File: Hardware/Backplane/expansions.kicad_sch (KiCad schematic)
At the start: 8 parts, among them U102 TCA9548APWR, U2901 P2X8C4M64P, U3001 NL17SZS11DFT2G-Q, U3002 NL17SZS11DFT2G-Q

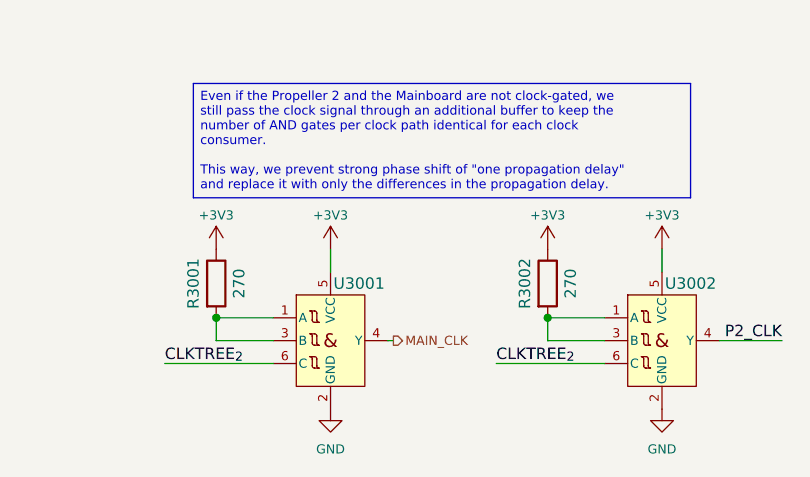
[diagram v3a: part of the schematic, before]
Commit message: Cleans up schematic even more, consolidates 270 and 100 Ohm resistors into the 560 ohm resistor, as they were only used as series resistors for the mosfets and LED current limiters
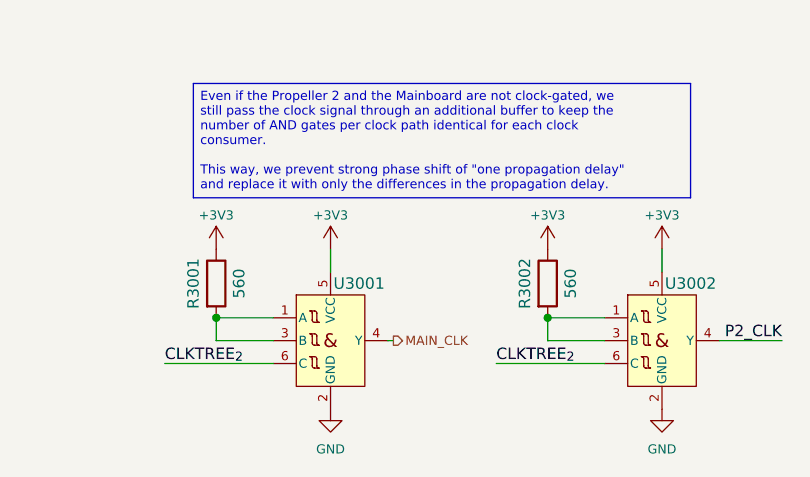
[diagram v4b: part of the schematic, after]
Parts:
- R3001, R3002: value 270 -> 560; Digikey Part No RMCF0603FT270RCT-ND -> RR08P560DCT-ND
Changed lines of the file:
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@@
 			)
 		)
-		(property "Value" "270"
+		(property "Value" "560"
 			(at 85.09 174.625 90)
 			(effects
@@
 			)
 		)
-		(property "Datasheet" "https://www.seielect.com/catalog/SEI-RMCF_RMCP.pdf"
+		(property "Datasheet" "https://www.susumu.co.jp/common/pdf/n_catalog_partition05_en.pdf"
 			(at 82.55 174.625 0)
 			(effects
@@
 			)
 		)
-		(property "Digikey Part No" "RMCF0603FT270RCT-ND"
+		(property "Digikey Part No" "RR08P560DCT-ND"
 			(at 82.55 174.625 90)
 			(effects
@@
 			)
 		)
-		(property "Value" "270"
+		(property "Value" "560"
 			(at 121.92 174.625 90)
 			(effects
@@
 			)
 		)
-		(property "Datasheet" "https://www.seielect.com/catalog/SEI-RMCF_RMCP.pdf"
+		(property "Datasheet" "https://www.susumu.co.jp/common/pdf/n_catalog_partition05_en.pdf"
 			(at 119.38 174.625 0)
 			(effects
@@
 			)
 		)
-		(property "Digikey Part No" "RMCF0603FT270RCT-ND"
+		(property "Digikey Part No" "RR08P560DCT-ND"
 			(at 119.38 174.625 90)
 			(effects

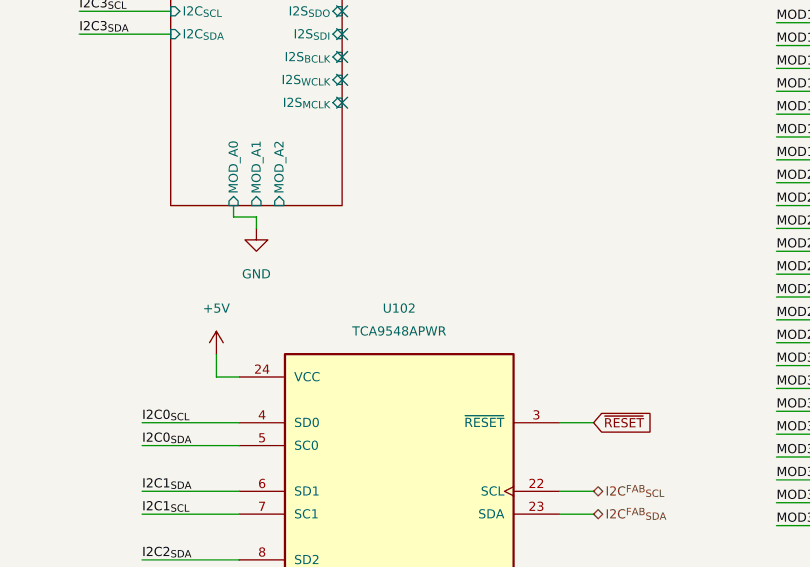
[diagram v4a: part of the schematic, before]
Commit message: More BOM consolidation
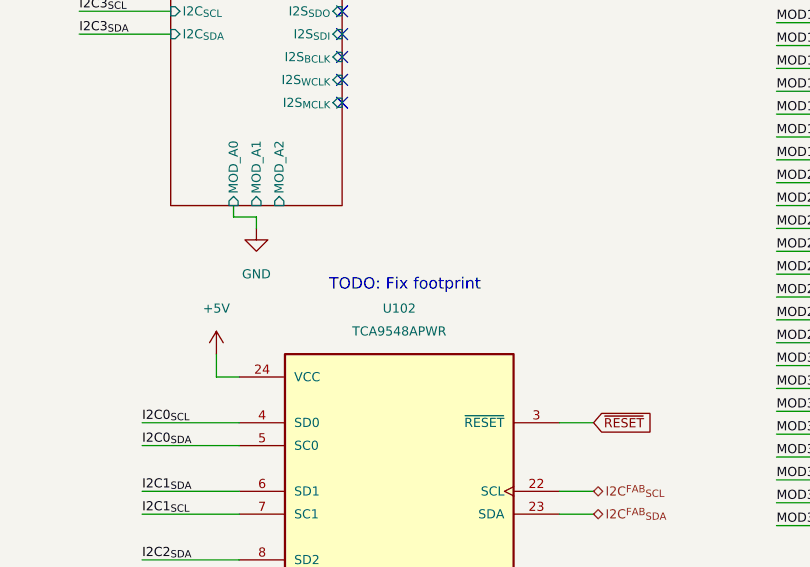
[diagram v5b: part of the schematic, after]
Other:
- note added: "TODO: Fix footprint"
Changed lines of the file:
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@@
 		(company "Ashet Technologies")
+	)
+	(text "TODO: Fix footprint"
+		(exclude_from_sim no)
+		(at 184.785 81.28 0)
+		(effects
+			(font
+				(size 1.27 1.27)
+			)
+		)
 	)
 	(text_box "Even if the Propeller 2 and the Mainboard are not clock-gated, we still pass the clock signal through an additional buffer to keep the number of AND gates per clock path identical for each clock consumer.\n\nThis way, we prevent strong phase shift of \"one propagation delay\" and replace it with only the differences in the propagation delay."

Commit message: Upgrades schematic files to KiCAD 10.0
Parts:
- U3001, U3002: DigiKey Part No 488-NL17SZS11DFT2G-QCT-ND -> (none); Digikey Part No (none) -> 488-NL17SZS11DFT2G-QCT-ND

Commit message: Further backplane PCB cleanup.
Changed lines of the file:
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@@
+	(wire
+		(pts
+			(xy 0.0762 0.0762) (xy 47.0662 0.0762)
+		)
+		(stroke
+			(width 0)
+			(type default)
+		)
+	)
 	(wire
 		(pts
@@
 		)
 		(stroke
+			(width 0)
+			(type default)
+		)
+	)
+	(wire
+		(pts
+			(xy 1.3462 1.3462) (xy 48.3362 1.3462)
+		)
+		(stroke
+			(width 0)
+			(type default)
+		)
+	)
+	(wire
+		(pts
+			(xy 0.0762 2.6162) (xy 47.0662 2.6162)
+		)
+		(stroke

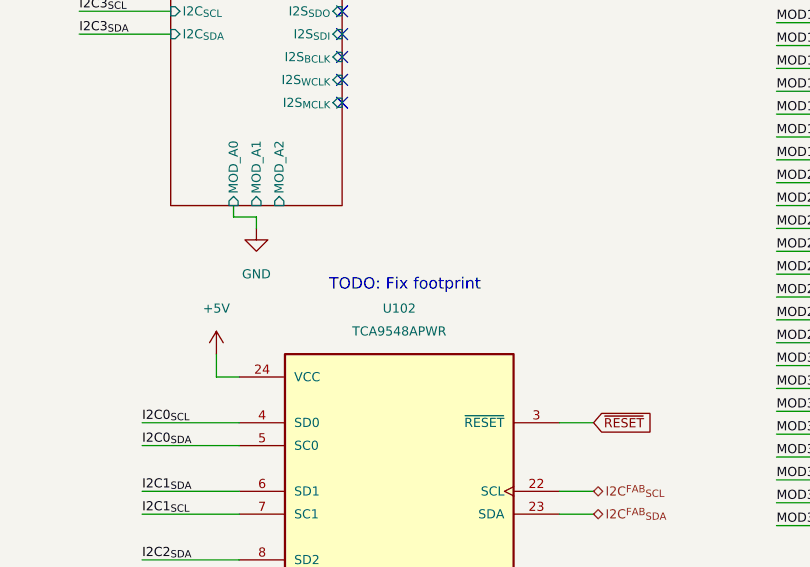
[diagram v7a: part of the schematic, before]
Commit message: Backplane: Fixes missing footprints/parts, starts to work on the layout seriously.
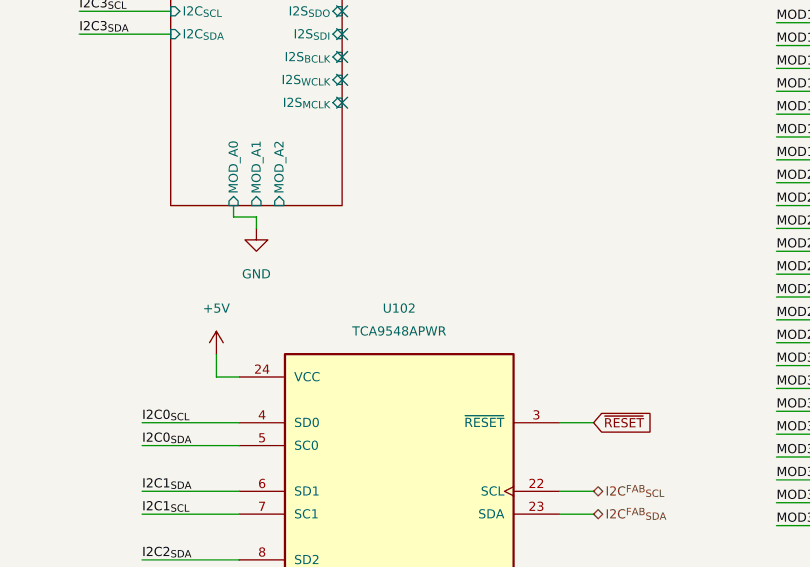
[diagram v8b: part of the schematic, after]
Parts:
- U102: footprint TCA9548APWR:SOP65P640X120-24N -> Home Computer:TCA9548APWR
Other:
- note removed: "TODO: Fix footprint"
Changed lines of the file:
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@@
 		(company "Ashet Technologies")
 	)
-	(text "TODO: Fix footprint"
-		(exclude_from_sim no)
-		(at 184.785 81.28 0)
-		(effects
-			(font
-				(size 1.27 1.27)
-			)
-		)
-	)
 	(text_box "Even if the Propeller 2 and the Mainboard are not clock-gated, we still pass the clock signal through an additional buffer to keep the number of AND gates per clock path identical for each clock consumer.\n\nThis way, we prevent strong phase shift of \"one propagation delay\" and replace it with only the differences in the propagation delay."
 		(exclude_from_sim no)
@@
 			)
 		)
-		(property "Footprint" "TCA9548APWR:SOP65P640X120-24N"
+		(property "Footprint" "Home Computer:TCA9548APWR"
 			(at 184.15 124.46 0)
 			(hide yes)
